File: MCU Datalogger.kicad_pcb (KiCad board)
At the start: 2 copper layers, 29 parts, among them J1 Conn_01x04_Pin, J2 Conn_01x09_Pin, J3 Conn_01x04_Pin, J4 Conn_02x03_Odd_Even, U1 24LC1025, U2 24LC1025, U3 DS1337S_, U4 ATMEGA328P-AU, Y1 32.768 KHz, Y2 16 MHz

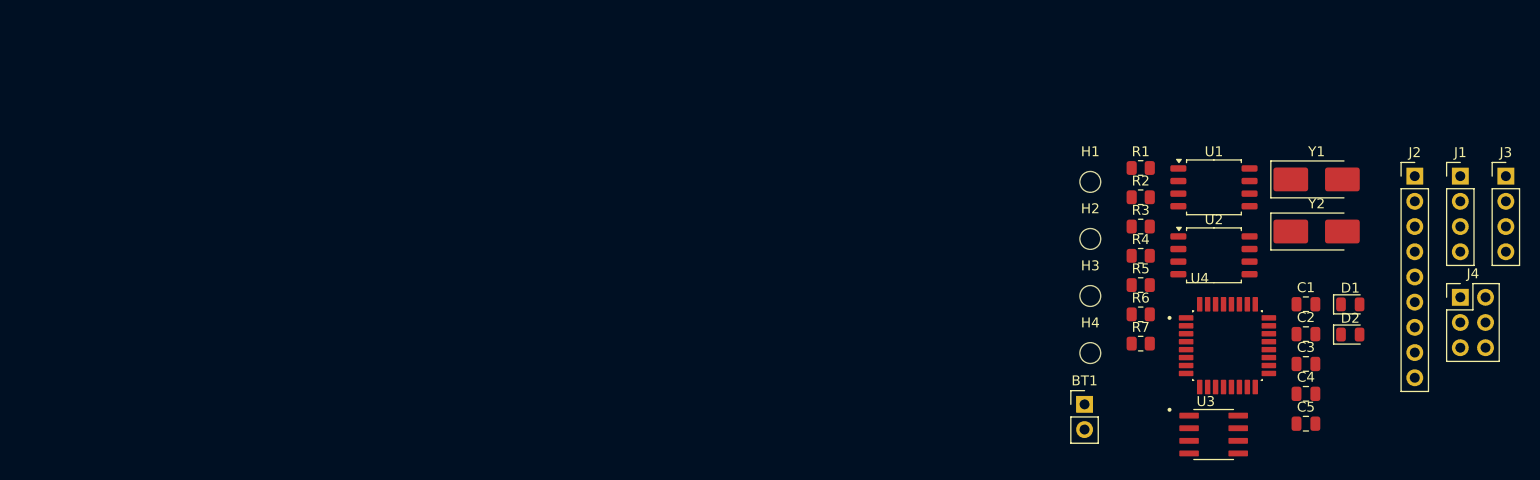
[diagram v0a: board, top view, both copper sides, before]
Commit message: Completed Placements of Footprints
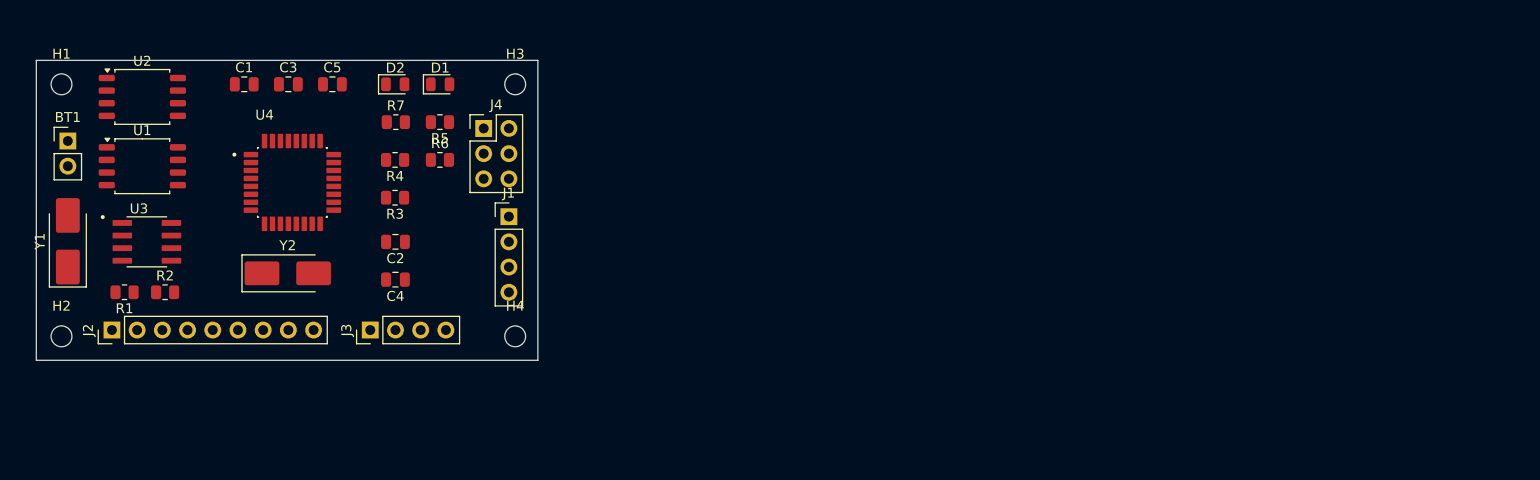
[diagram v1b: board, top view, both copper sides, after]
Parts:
- moved J2 132.2 mm to (72.4, 95.2), turned to 90 degrees
- moved Y1 126.0 mm to (67.9, 86.3), turned to 90 degrees
- moved J3 115.5 mm to (98.4, 95.2), turned to 90 degrees
- moved C1 109.3 mm to (85.7, 70.5)
- moved U3 109.3 mm to (75.9, 86.4)
- moved U2 109.2 mm to (75.5, 71.8)
- moved U1 108.0 mm to (75.5, 78.7)
- moved C3 106.4 mm to (90.2, 70.5)
- moved BT1 105.8 mm to (67.9, 76.2)
- moved H1 104.1 mm to (67.3, 70.5)
- moved H2 104.1 mm to (67.3, 95.9)
- moved C5 103.9 mm to (94.6, 70.5)
- moved Y2 103.8 mm to (90.1, 89.5)
- moved R1 103.2 mm to (73.7, 91.4), turned to 180 degrees
- moved J4 99.9 mm to (109.9, 74.9)
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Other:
- board outline added: 50.5 x 30.2 mm

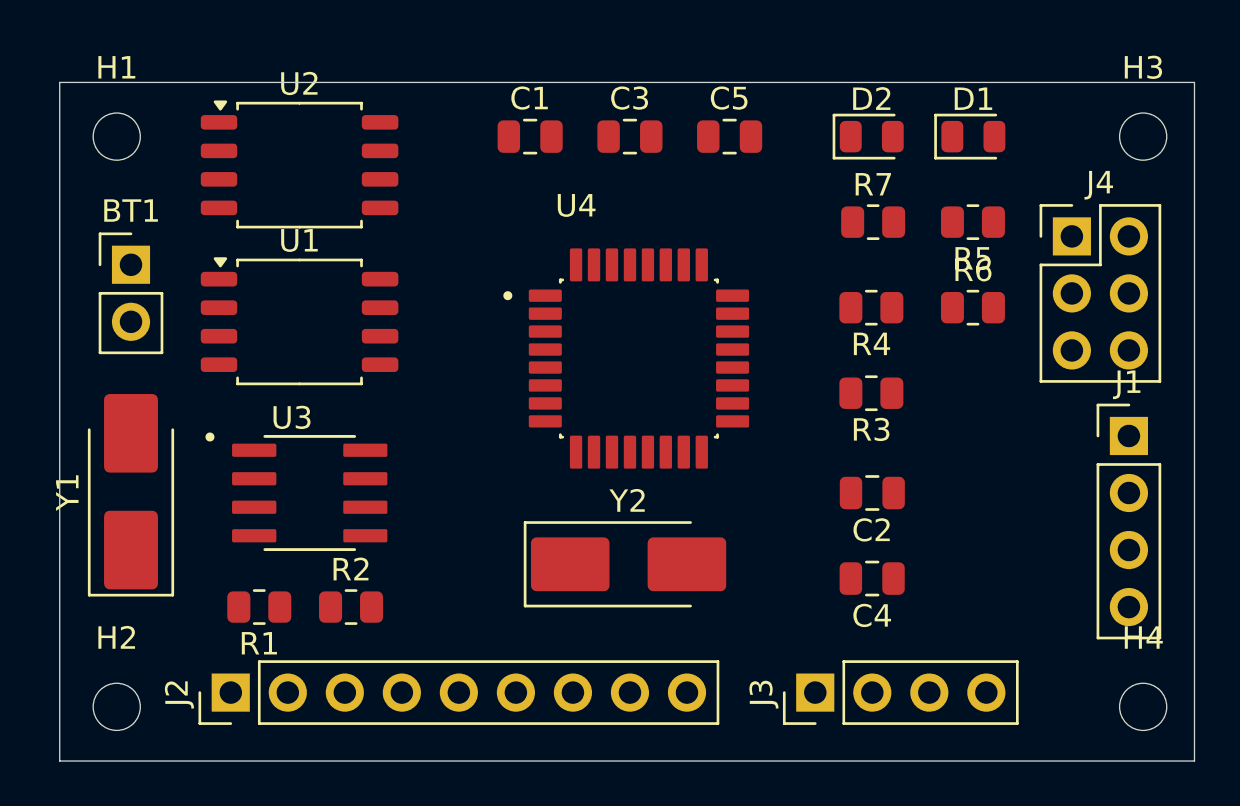
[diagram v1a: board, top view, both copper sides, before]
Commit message: Routing sans GND Vcc complete
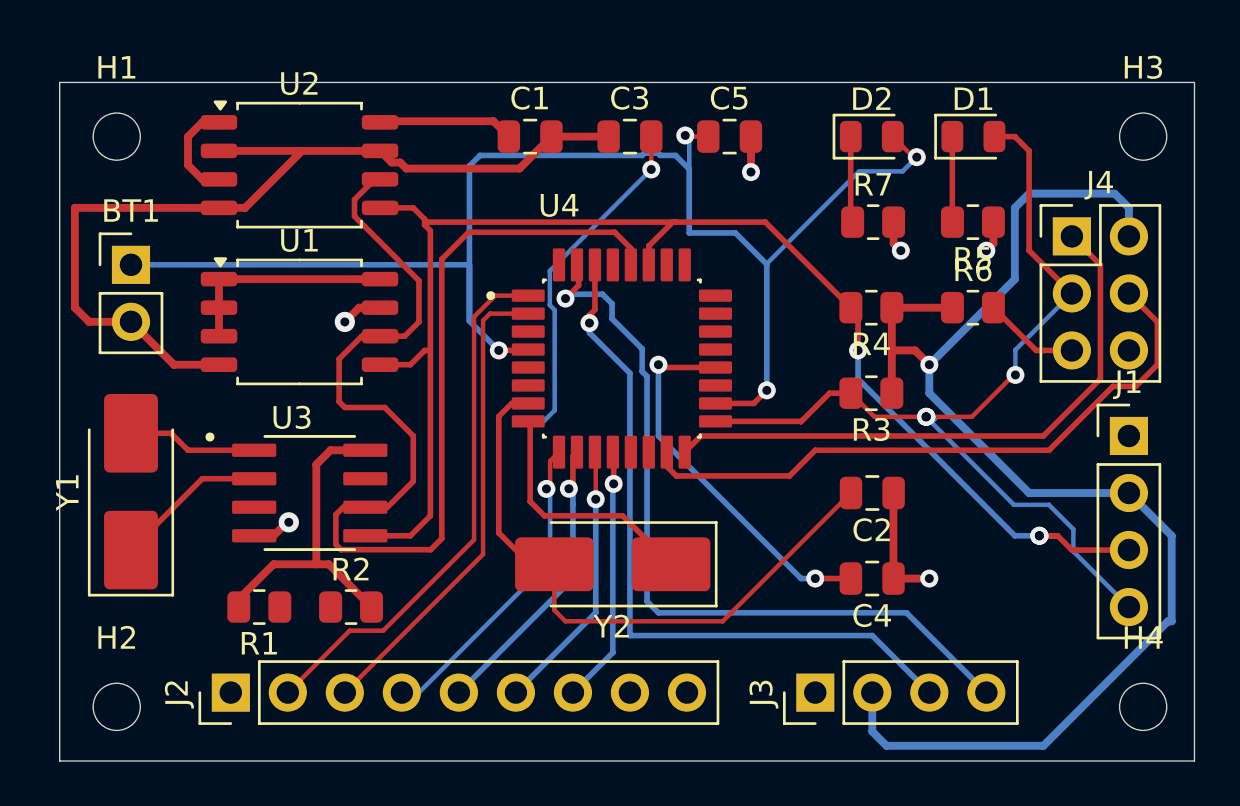
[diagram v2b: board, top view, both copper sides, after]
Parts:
- moved U4 0.76 mm to (89.8, 80.4)
- moved Y2 0.71 mm to (89.4, 89.5), turned to 180 degrees
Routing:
- net /Vcc: track 0.00 -> 94.9 mm, vias 0 -> 1
- net /SCK: track 0.00 -> 94.9 mm, vias 0 -> 3
- net Net-(BT1-+): track 0.00 -> 68.6 mm, vias 0 -> 4
- net /SDA: track 0.00 -> 63.7 mm, vias 0 -> 3
- net GND: track 0.00 -> 54.9 mm, vias 0 -> 6
- net /TX: track 0.00 -> 34.8 mm, vias 0 -> 1
- net /RX: track 0.00 -> 31.7 mm, vias 0 -> 1
- net Net-(U4-PB6): track 0.00 -> 28.5 mm
- net /MOSI: track 0.00 -> 28.4 mm
- net /MISO: track 0.00 -> 26.7 mm
- net Net-(U4-PB7): track 0.00 -> 26.2 mm, vias 0 -> 1
- net /D3: track 0.00 -> 23.9 mm
- net /D4: track 0.00 -> 21.7 mm
- net Net-(U4-AREF): track 0.00 -> 17.0 mm, vias 0 -> 2
- net /D5: track 0.00 -> 14.2 mm, vias 0 -> 1
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
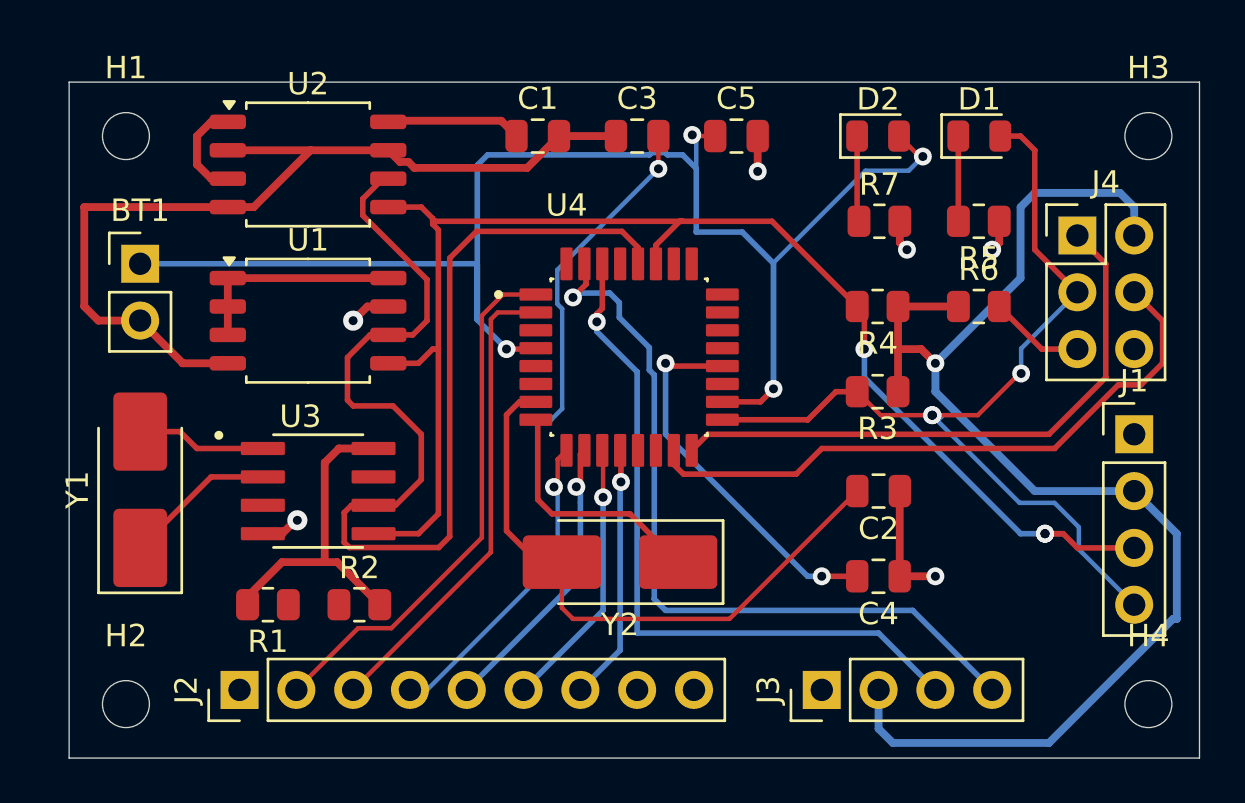
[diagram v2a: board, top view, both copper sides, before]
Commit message: Routing sans GND Vcc complete.
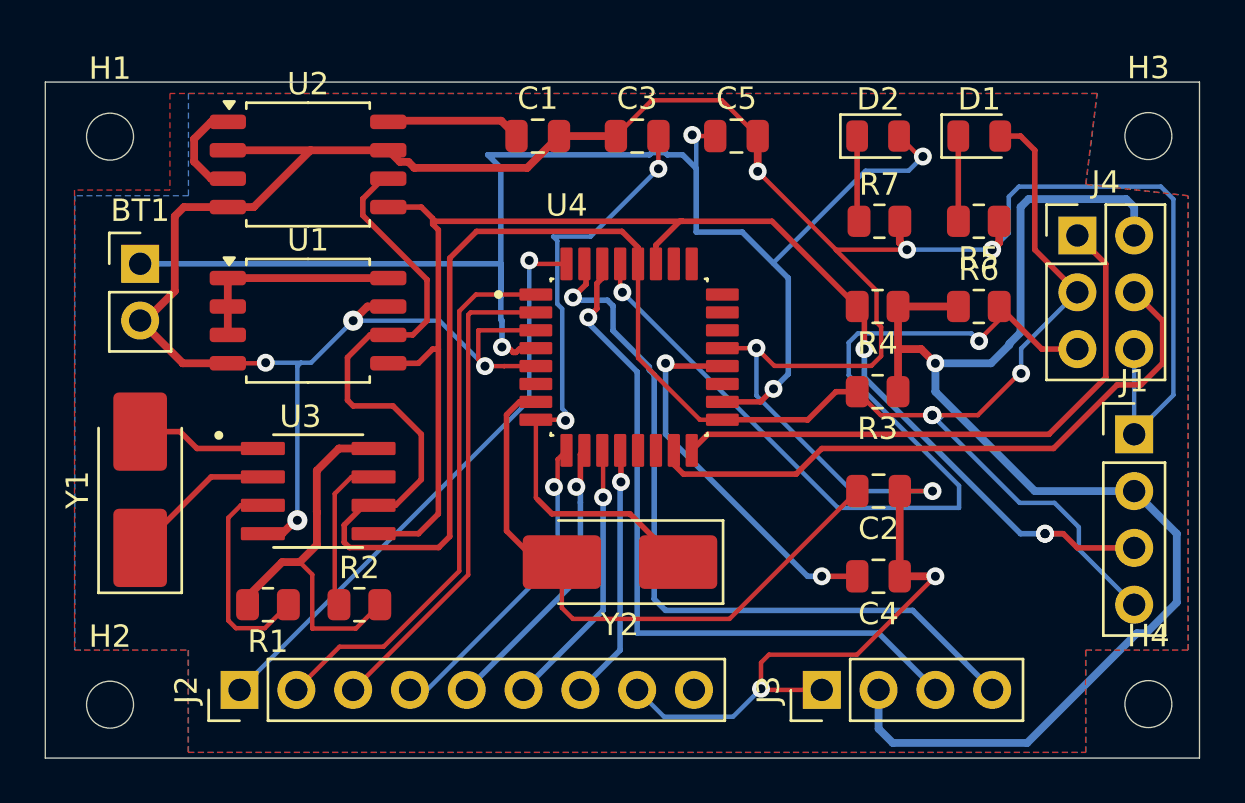
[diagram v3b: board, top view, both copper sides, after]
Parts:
- moved H1 0.71 mm to (66.6, 70.5)
- moved H2 0.71 mm to (66.6, 95.9)
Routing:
- net GND: track 54.9 -> 167.5 mm, vias 6 -> 11
- net /RESET: track 4.28 -> 42.7 mm, vias 0 -> 2
- net /D2: track 0.06 -> 26.4 mm, vias 0 -> 1
- net Net-(U3-~{INTA}): track 0.00 -> 9.64 mm
- net /SCK: track 94.9 -> 103.7 mm
- net Net-(U3-SQW/~INT): track 0.00 -> 7.09 mm
- net /Vcc: track 94.9 -> 98.6 mm
- net Net-(U4-PB7): track 26.2 -> 28.4 mm, vias 1 -> 2
- net /D3: track 23.9 -> 24.8 mm
- net /D4: track 21.7 -> 22.4 mm
- added copper zone on B.Cu, net (none)
- added copper zone on F.Cu, net /Vcc
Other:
- board size 50.5 x 30.2 mm -> 51.6 x 30.2 mm
